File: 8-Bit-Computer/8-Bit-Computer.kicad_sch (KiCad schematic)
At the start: 71 parts, among them J1 XLR3_Switched, J2 XLR3_Switched, SW1 SW_Push, SW2 SW_DIP_x04, SW3 SW_DIP_x08, SW4 SW_Push, U1 NA555D, U10 74LS283, U11 74HC245, U12 74HC86, U13 74HC86, U14 74HC245, U15 HM62256BLP, U16 74HC245, U17 74157, U18 74157, U19 74157, U2 AMS1117-5.0, U20 74HC00, U21 74157, U22 74173, U3 74HC00, U4 LM555xM, U5 NA555D, U6 74HC00, U7 74HC245, U8 74HC245, U9 74LS283

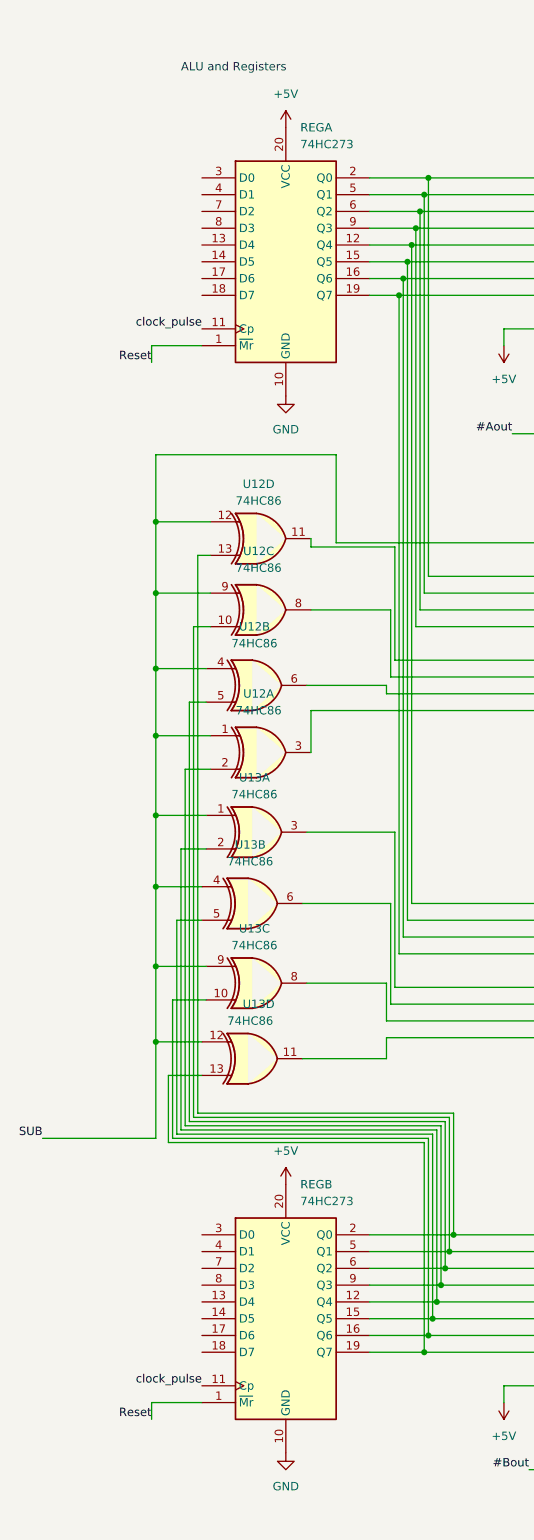
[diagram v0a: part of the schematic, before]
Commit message: changed register chips to 74ls377
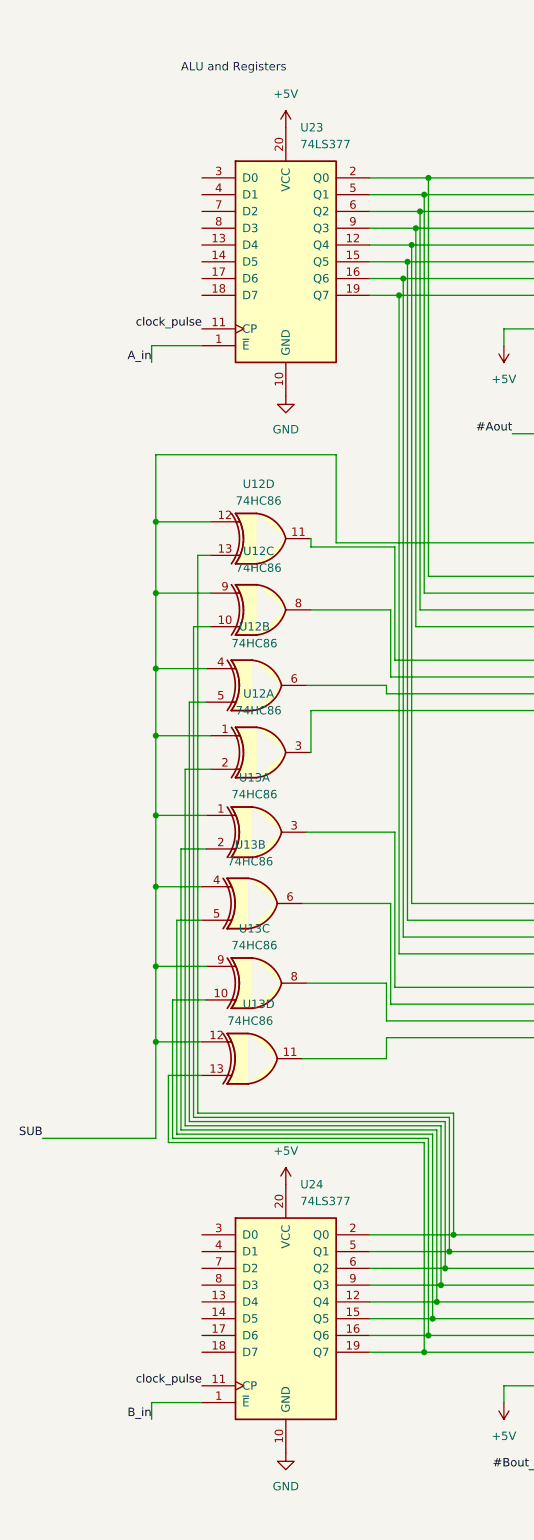
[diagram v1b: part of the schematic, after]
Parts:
- removed REGA, REGB: 74HC273, symbol 74xx:74HC273
- added U23, U24: 74LS377, symbol 74xx:74LS377
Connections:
- net +5V: now also U23.20 (VCC), U24.20 (VCC)
- net GND: now also U23.10 (GND), U24.10 (GND)
- net clock_pulse: now also U23.11 (CP), U24.11 (CP)
- net at U12.2, U8.5 (A3): now also U24.9 (Q3)
- net at U13.2, U8.6 (A4): now also U24.12 (Q4)
- net at U13.5, U8.7 (A5): now also U24.15 (Q5)
- net at U13.10, U8.8 (A6): now also U24.16 (Q6)
- net at U13.13, U8.9 (A7): now also U24.19 (Q7)
- net at U12.13, U8.2 (A0): now also U24.2 (Q0)
- net at U12.10, U8.3 (A1): now also U24.5 (Q1)
- net at U12.5, U8.4 (A2): now also U24.6 (Q2)
- net at U7.2 (A0), U9.5 (A1): now also U23.2 (Q0)
- net at U7.3 (A1), U9.3 (A2): now also U23.5 (Q1)
- net at U7.4 (A2), U9.14 (A3): now also U23.6 (Q2)
- net at U7.5 (A3), U9.12 (A4): now also U23.9 (Q3)
- net at U10.5 (A1), U7.6 (A4): now also U23.12 (Q4)
- net at U10.3 (A2), U7.7 (A5): now also U23.15 (Q5)
- net at U10.14 (A3), U7.8 (A6): now also U23.16 (Q6)
- net at U10.12 (A4), U7.9 (A7): now also U23.19 (Q7)
- new net A_in: U23.1 (~{E})
- new net B_in: U24.1 (~{E})
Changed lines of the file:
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@@
     (effects (font (size 1.27 1.27)) (justify right bottom))
   )
-  (label "Reset" (at 38.1 455.93 180) (fields_autoplaced)
+  (label "B_in" (at 38.1 455.93 180) (fields_autoplaced)
     (effects (font (size 1.27 1.27)) (justify right bottom))
   )
@@
     (effects (font (size 1.27 1.27)) (justify right bottom))
   )
-  (label "Reset" (at 38.1 295.91 180) (fields_autoplaced)
+  (label "A_in" (at 38.1 295.91 180) (fields_autoplaced)
     (effects (font (size 1.27 1.27)) (justify right bottom))
   )
@@
     )
   )
-  (symbol (lib_id "power:+5V") (at 711.835 352.425 270) (unit 1)
-    (in_bom yes) (on_board yes) (dnp no) (fields_autoplaced)
-    (property "Reference" "#PWR099" (at 708.025 352.425 0)
-      (effects (font (size 1.27 1.27)) hide)
-    )
-    (property "Value" "+5V" (at 715.01 352.425 90)
-      (effects (font (size 1.27 1.27)) (justify left))
-    )
-    (property "Footprint" "" (at 711.835 352.425 0)
-      (effects (font (size 1.27 1.27)) hide)
-    )
-    (property "Datasheet" "" (at 711.835 352.425 0)
-      (effects (font (size 1.27 1.27)) hide)
-    )
-    (pin "1")
-    (instances
-      (project "8-Bit-Computer"
-        (path "/7068cf22-ceca-4c5f-b7d5-56f579bc3b1d"
-          (reference "#PWR099") (unit 1)
-        )
-      )
-    )
-  )
-  (symbol (lib_id "74xx:74HC273") (at 58.42 440.69 0) (unit 1)
-    (in_bom yes) (on_board yes) (dnp no)
-    (property "Reference" "REGB" (at 60.6141 420.37 0)
-      (effects (font (size 1.27 1.27)) (justify left))
-    )
-    (property "Value" "74HC273" (at 60.6141 422.91 0)
-      (effects (font (size 1.27 1.27)) (justify left))
-    )
-    (property "Footprint" "" (at 58.42 440.69 0)
-      (effects (font (size 1.27 1.27)) hide)
-    )
-    (property "Datasheet" "https://assets.nexperia.com/documents/data-sheet/74HC_HCT273.pdf" (at 58.42 440.69 0)
-      (effects (font (size 1.27 1.27)) hide)
-    )
-    (pin "3")
-    (pin "20")
-    (pin "6")
-    (pin "5")
+  (symbol (lib_id "74xx:74LS377") (at 58.42 280.67 0) (unit 1)
+    (in_bom yes) (on_board yes) (dnp no) (fields_autoplaced)
+    (property "Reference" "U23" (at 60.6141 260.35 0)
+      (effects (font (size 1.27 1.27)) (justify left))
+    )
+    (property "Value" "74LS377" (at 60.6141 262.89 0)
+      (effects (font (size 1.27 1.27)) (justify left))
+    )
+    (property "Footprint" "" (at 58.42 280.67 0)
+      (effects (font (size 1.27 1.27)) hide)
+    )
+    (property "Datasheet" "http://www.ti.com/lit/gpn/sn74LS377" (at 58.42 280.67 0)
+      (effects (font (size 1.27 1.27)) hide)
+    )
     (pin "19")
-    (pin "8")
-    (pin "16")
-    (pin "18")
-    (pin "1")
-    (pin "17")
     (pin "15")
     (pin "14")
+    (pin "4")
+    (pin "5")
+    (pin "17")
+    (pin "2")
+    (pin "8")
+    (pin "7")
+    (pin "18")
+    (pin "9")
+    (pin "6")
     (pin "13")
-    (pin "7")
-    (pin "4")
-    (pin "2")
-    (pin "9")
+    (pin "16")
+    (pin "20")
+    (pin "3")
+    (pin "1")
     (pin "11")
     (pin "12")
@@
       (project "8-Bit-Computer"
         (path "/7068cf22-ceca-4c5f-b7d5-56f579bc3b1d"
-          (reference "REGB") (unit 1)
+          (reference "U23") (unit 1)
+        )
+      )
+    )
+  )
+  (symbol (lib_id "power:+5V") (at 711.835 352.425 270) (unit 1)
+    (in_bom yes) (on_board yes) (dnp no) (fields_autoplaced)
+    (property "Reference" "#PWR099" (at 708.025 352.425 0)
+      (effects (font (size 1.27 1.27)) hide)
+    )
+    (property "Value" "+5V" (at 715.01 352.425 90)
+      (effects (font (size 1.27 1.27)) (justify left))
+    )
+    (property "Footprint" "" (at 711.835 352.425 0)
+      (effects (font (size 1.27 1.27)) hide)
+    )
+    (property "Datasheet" "" (at 711.835 352.425 0)
+      (effects (font (size 1.27 1.27)) hide)
+    )
+    (pin "1")
+    (instances
+      (project "8-Bit-Computer"
+        (path "/7068cf22-ceca-4c5f-b7d5-56f579bc3b1d"
+          (reference "#PWR099") (unit 1)
         )
       )
@@
     )
   )
-  (symbol (lib_id "74xx:74HC273") (at 58.42 280.67 0) (unit 1)
-    (in_bom yes) (on_board yes) (dnp no)
-    (property "Reference" "REGA" (at 60.6141 260.35 0)
-      (effects (font (size 1.27 1.27)) (justify left))
-    )
-    (property "Value" "74HC273" (at 60.6141 262.89 0)
-      (effects (font (size 1.27 1.27)) (justify left))
-    )
-    (property "Footprint" "" (at 58.42 280.67 0)
-      (effects (font (size 1.27 1.27)) hide)
-    )
-    (property "Datasheet" "https://assets.nexperia.com/documents/data-sheet/74HC_HCT273.pdf" (at 58.42 280.67 0)
-      (effects (font (size 1.27 1.27)) hide)
-    )
-    (pin "3")
-    (pin "20")
-    (pin "6")
-    (pin "5")
+  (symbol (lib_id "74xx:74LS377") (at 58.42 440.69 0) (unit 1)
+    (in_bom yes) (on_board yes) (dnp no) (fields_autoplaced)
+    (property "Reference" "U24" (at 60.6141 420.37 0)
+      (effects (font (size 1.27 1.27)) (justify left))
+    )
+    (property "Value" "74LS377" (at 60.6141 422.91 0)
+      (effects (font (size 1.27 1.27)) (justify left))
+    )
+    (property "Footprint" "" (at 58.42 440.69 0)
+      (effects (font (size 1.27 1.27)) hide)
+    )
+    (property "Datasheet" "http://www.ti.com/lit/gpn/sn74LS377" (at 58.42 440.69 0)
+      (effects (font (size 1.27 1.27)) hide)
+    )
     (pin "19")
-    (pin "8")
-    (pin "16")
-    (pin "18")
-    (pin "1")
-    (pin "17")
     (pin "15")
     (pin "14")
+    (pin "4")
+    (pin "5")
+    (pin "17")
+    (pin "2")
+    (pin "8")
+    (pin "7")
+    (pin "18")
+    (pin "9")
+    (pin "6")
     (pin "13")
-    (pin "7")
-    (pin "4")
-    (pin "2")
-    (pin "9")
+    (pin "16")
+    (pin "20")
+    (pin "3")
+    (pin "1")
     (pin "11")
     (pin "12")
@@
       (project "8-Bit-Computer"
         (path "/7068cf22-ceca-4c5f-b7d5-56f579bc3b1d"
-          (reference "REGA") (unit 1)
-        )
-      )
+          (reference "U24") (unit 1)
+        )
+      )

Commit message: will be back at it
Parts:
- added D10, D2, D8, D9: G_LED, symbol Device:LED
- added D11: B_LED, symbol Device:LED
- added R27, R28, R29, R30, R31: R_US, symbol Device:R_US
- added U25: 74LS377, symbol 74xx:74LS377
- added U26, U28: 74HC245, symbol 74xx:74HC245
- added U27: 74LS161, symbol 74xx:74LS161
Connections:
- net +5V: now also U25.20 (VCC), U26.1 (A->B), U26.20 (VCC), U27.16 (VCC), U28.1 (A->B), U28.20 (VCC)
- net GND: now also D10.1 (K), D11.1 (K), D2.1 (K), D8.1 (K), D9.1 (K), U25.10 (GND), U26.10 (GND), U27.8 (GND), U28.10 (GND)
- net clock_pulse: now also R31.1, U25.11 (CP)
- new net: R29.1, U27.13 (Q1), U28.3 (A1)
- new net: R28.1, U27.12 (Q2), U28.4 (A2)
- new net: R27.1, U27.11 (Q3), U28.5 (A3)
- new net: U25.12 (Q4), U26.6 (A4)
- new net: U25.15 (Q5), U26.7 (A5)
- new net: U25.16 (Q6), U26.8 (A6)
- new net: U25.19 (Q7), U26.9 (A7)
- new net: U25.2 (Q0), U26.2 (A0)
- new net: U25.5 (Q1), U26.3 (A1)
- new net: U25.6 (Q2), U26.4 (A2)
- new net: U25.9 (Q3), U26.5 (A3)
- new net: D10.2 (A), R30.2
- new net: D8.2 (A), R28.2
- new net: D9.2 (A), R29.2
- new net: D11.2 (A), R31.2
- new net: D2.2 (A), R27.2
- new net #InstrReg_in: U25.1 (~{E})
- new net #InstrReg_out: U26.19 (CE)
- new net #PC_out: U28.19 (CE)
- new net LSB: R30.1, U27.14 (Q0), U28.2 (A0)
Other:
- note added: "Instruction Register"
- moved on the sheet: U10, U11, U12A, U12B, U12C, U12D, U12E, U13A, U13B, U13C, U13D, U13E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

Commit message: gbti
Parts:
- added U29: HDSP-7503, Display_7Segment:HDSP-A151, symbol Display_Character:HDSP-7503
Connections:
- net GND: now also U28.6 (A4), U28.7 (A5), U28.8 (A6), U28.9 (A7)
- net clock_pulse: now also U27.2 (CP)
- net count_enable: now reaches U27.10 (CET)
- net count_enable: now also U27.7 (CEP)
- net #J: now reaches U27.9 (~{PE})
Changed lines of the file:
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@@
   (junction (at 85.09 490.855) (diameter 0) (color 0 0 0 0)
   )
+  (junction (at 43.18 251.46) (diameter 0) (color 0 0 0 0)
+  )
   (junction (at 650.875 309.245) (diameter 0) (color 0 0 0 0)
   )
@@
   (junction (at 74.93 238.76) (diameter 0) (color 0 0 0 0)
   )
+  (junction (at 43.18 246.38) (diameter 0) (color 0 0 0 0)
+  )
   (junction (at 80.01 335.915) (diameter 0) (color 0 0 0 0)
   )
@@
   (junction (at 291.465 86.36) (diameter 0) (color 0 0 0 0)
   )
+  (junction (at 114.935 248.92) (diameter 0) (color 0 0 0 0)
+  )
   (junction (at 86.995 483.235) (diameter 0) (color 0 0 0 0)
   )
@@
   (junction (at 88.9 236.22) (diameter 0) (color 0 0 0 0)
   )
+  (junction (at 114.935 243.84) (diameter 0) (color 0 0 0 0)
+  )
   (junction (at 79.375 338.455) (diameter 0) (color 0 0 0 0)
   )
@@
   (junction (at 687.705 235.585) (diameter 0) (color 0 0 0 0)
   )
+  (junction (at 114.935 246.38) (diameter 0) (color 0 0 0 0)
+  )
   (junction (at 85.725 488.315) (diameter 0) (color 0 0 0 0)
   )
@@
     (stroke (width 0) (type default))
   )
+  (wire (pts (xy 22.225 251.46) (xy 43.18 251.46))
+    (stroke (width 0) (type default))
+  )
   (wire (pts (xy 227.33 83.82) (xy 250.825 83.82))
     (stroke (width 0) (type default))
@@
     (stroke (width 0) (type default))
   )
+  (wire (pts (xy 27.94 246.38) (xy 43.18 246.38))
+    (stroke (width 0) (type default))
+  )
   (wire (pts (xy 795.02 210.82) (xy 795.02 256.54))
     (stroke (width 0) (type default))
@@
     (stroke (width 0) (type default))
   )
+  (wire (pts (xy 114.935 243.84) (xy 114.935 246.38))
+    (stroke (width 0) (type default))
+  )
   (wire (pts (xy 168.91 71.12) (xy 171.45 71.12))
     (stroke (width 0) (type default))
@@
     (stroke (width 0) (type default))
   )
+  (wire (pts (xy 43.18 243.84) (xy 22.225 243.84))
+    (stroke (width 0) (type default))
+  )
   (wire (pts (xy 125.73 64.77) (xy 133.35 64.77))
     (stroke (width 0) (type default))
@@
     (stroke (width 0) (type default))
   )
+  (wire (pts (xy 114.935 241.3) (xy 114.935 243.84))
+    (stroke (width 0) (type default))
+  )
   (wire (pts (xy 128.27 391.16) (xy 128.27 418.465))
     (stroke (width 0) (type default))
@@
     (stroke (width 0) (type default))
   )
+  (wire (pts (xy 43.18 251.46) (xy 43.815 251.46))
+    (stroke (width 0) (type default))
+  )
   (wire (pts (xy 134.62 417.195) (xy 161.29 417.195))
     (stroke (width 0) (type default))
@@
     (stroke (width 0) (type default))
   )
+  (wire (pts (xy 114.935 246.38) (xy 114.935 248.92))
+    (stroke (width 0) (type default))
+  )
   (wire (pts (xy 82.55 325.755) (xy 82.55 386.08))
     (stroke (width 0) (type default))
@@
     (stroke (width 0) (type default))
   )
+  (wire (pts (xy 43.18 246.38) (xy 43.18 248.92))
+    (stroke (width 0) (type default))
+  )
   (wire (pts (xy 747.395 248.92) (xy 687.07 248.92))
     (stroke (width 0) (type default))
@@
     (stroke (width 0) (type default))
   )
+  (wire (pts (xy 22.225 241.3) (xy 22.225 243.84))
+    (stroke (width 0) (type default))
+  )
   (wire (pts (xy 679.45 109.22) (xy 685.8 109.22))
     (stroke (width 0) (type default))
@@
     (effects (font (size 1.27 1.27)) (justify left bottom))
   )
-  (text "ALU and Registers" (at 720.09 449.58 0)
-    (effects (font (size 1.27 1.27)) (justify right bottom))
-  )
   (text "Instruction Register" (at 651.51 382.905 0)
     (effects (font (size 1.27 1.27)) (justify left bottom))
   )
+  (label "clock_pulse" (at 22.225 251.46 0) (fields_autoplaced)
+    (effects (font (size 1.27 1.27)) (justify left bottom))
+  )
   (label "clock_pulse" (at 516.89 328.295 180) (fields_autoplaced)
     (effects (font (size 1.27 1.27)) (justify right bottom))
@@
     (effects (font (size 1.27 1.27)) (justify right bottom))
   )
+  (label "#J" (at 22.225 241.3 180) (fields_autoplaced)
+    (effects (font (size 1.27 1.27)) (justify right bottom))
+  )
   (label "B_in" (at 41.275 511.175 180) (fields_autoplaced)
     (effects (font (size 1.27 1.27)) (justify right bottom))
@@
     (effects (font (size 1.27 1.27)) (justify right bottom))
   )
+  (label "count_enable" (at 27.94 246.38 180) (fields_autoplaced)
+    (effects (font (size 1.27 1.27)) (justify right bottom))
+  )
   (label "Addr_in" (at 575.31 152.4 180) (fields_autoplaced)
     (effects (font (size 1.27 1.27)) (justify right bottom))
@@
     )
   )
+  (symbol (lib_id "Display_Character:HDSP-7503") (at 211.455 508 0) (unit 1)
+    (in_bom yes) (on_board yes) (dnp no) (fields_autoplaced)
+    (property "Reference" "U29" (at 211.455 490.22 0)
+      (effects (font (size 1.27 1.27)))
+    )
+    (property "Value" "HDSP-7503" (at 211.455 492.76 0)
+      (effects (font (size 1.27 1.27)))
+    )
+    (property "Footprint" "Display_7Segment:HDSP-A151" (at 211.455 521.97 0)
+      (effects (font (size 1.27 1.27)) hide)
+    )
+    (property "Datasheet" "https://docs.broadcom.com/docs/AV02-2553EN" (at 201.295 494.03 0)
+      (effects (font (size 1.27 1.27)) hide)
+    )
+    (pin "10")
+    (pin "8")
+    (pin "9")
+    (pin "2")
+    (pin "3")
+    (pin "1")
+    (pin "4")
+    (pin "6")
+    (pin "7")
+    (pin "5")
+    (instances
+      (project "8-Bit-Computer"
+        (path "/7068cf22-ceca-4c5f-b7d5-56f579bc3b1d"
+          (reference "U29") (unit 1)
+        )
+      )
+    )
+  )
   (symbol (lib_id "Connector_Audio:XLR3_Switched") (at 116.205 196.215 90) (unit 2)
     (in_bom yes) (on_board yes) (dnp no) (fields_autoplaced)
@@
         )
       )
+    )
+  )
+  (symbol (lib_id "power:GND") (at 114.935 248.92 270) (unit 1)
+    (in_bom yes) (on_board yes) (dnp no) (fields_autoplaced)
+    (property "Reference" "#PWR0115" (at 108.585 248.92 0)
+      (effects (font (size 1.27 1.27)) hide)
+    )
+    (property "Value" "GND" (at 111.76 248.92 90)
+      (effects (font (size 1.27 1.27)) (justify right))
+    )
+    (property "Footprint" "" (at 114.935 248.92 0)
+      (effects (font (size 1.27 1.27)) hide)
+    )
+    (property "Datasheet" "" (at 114.935 248.92 0)
+      (effects (font (size 1.27 1.27)) hide)
+    )
+    (pin "1")
+    (instances
+      (project "8-Bit-Computer"
+        (path "/7068cf22-ceca-4c5f-b7d5-56f579bc3b1d"
+          (reference "#PWR0115") (unit 1)
+        )
+      )
